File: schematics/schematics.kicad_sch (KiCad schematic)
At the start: 40 parts, among them SW1 Reset, U4 PIC32MX170F256B

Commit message: Add motor STL
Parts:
- added D? (x2): Diode, symbol 218:Diode
- added L?: Inductor, symbol 218 spdl:Inductor
- added R_ext?: 22, symbol 218 spdl:Res1
- added R_int?: 34, symbol 218 spdl:Res1
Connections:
- net +5V: now also D?.1 (K)
- net GNDREF: now also D?.2 (A), R_ext?.2
- new net: L?.2, R_int?.1
- new net PWM (7544): D?.1 (K), D?.2 (A), L?.1
- new net Probe: R_ext?.1, R_int?.2
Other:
- note added: "Lab 7.1"
- note added: "Motor"

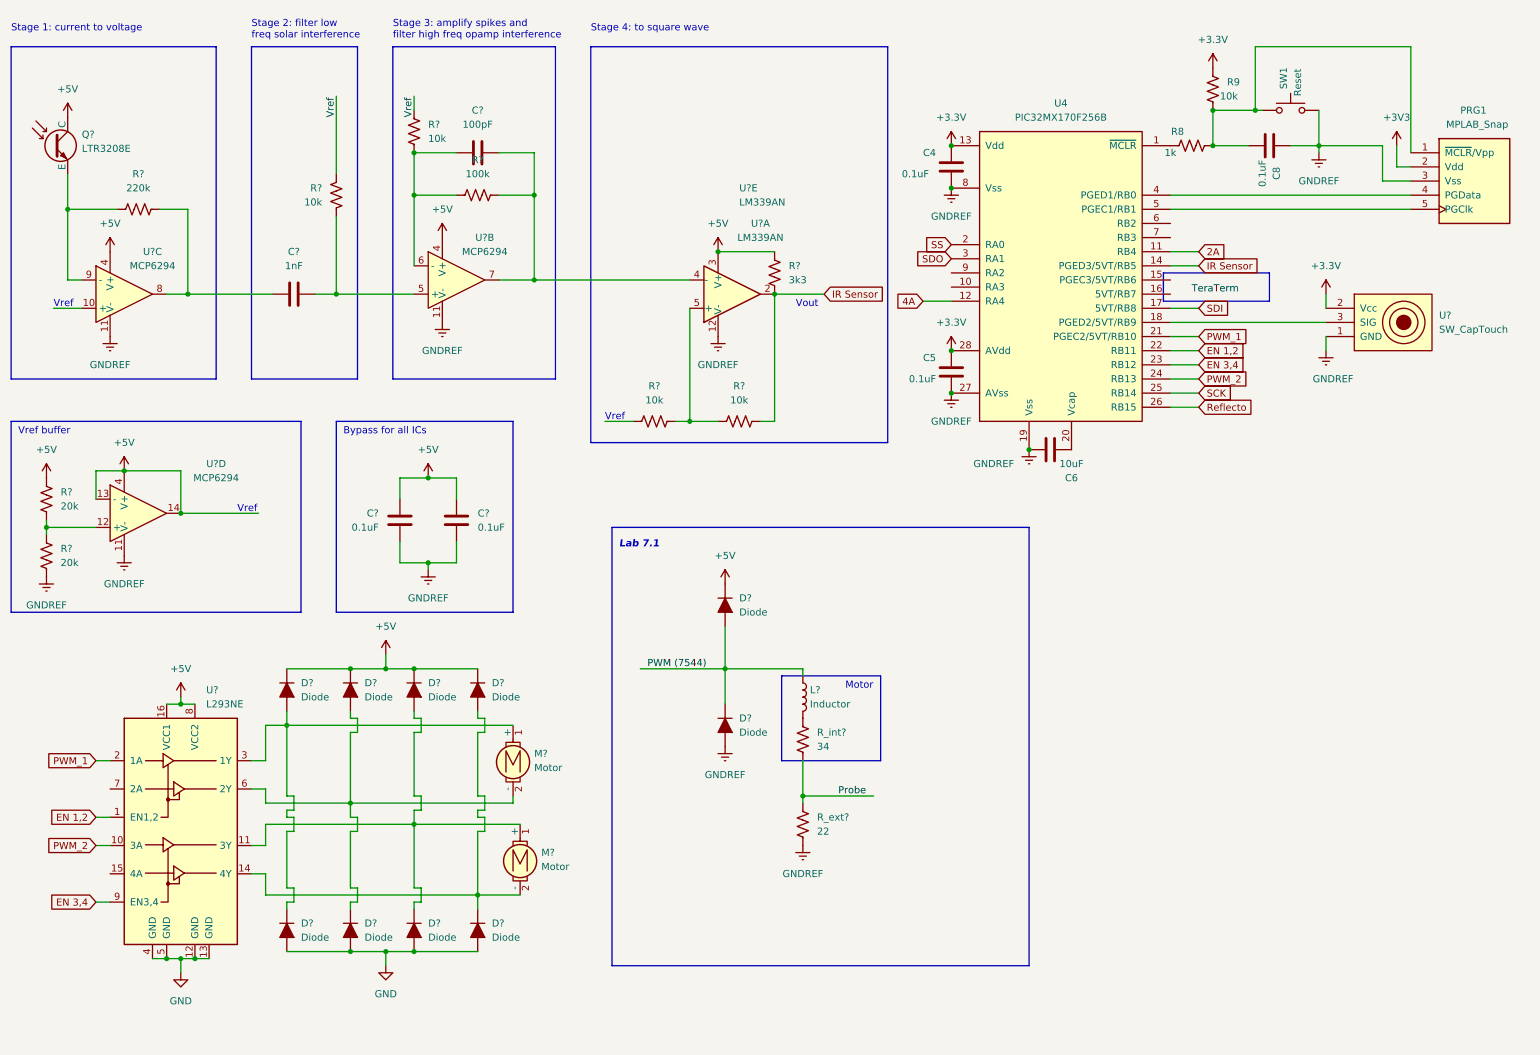
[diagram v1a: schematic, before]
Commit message: Update schematics and add new symbols to KiCAD
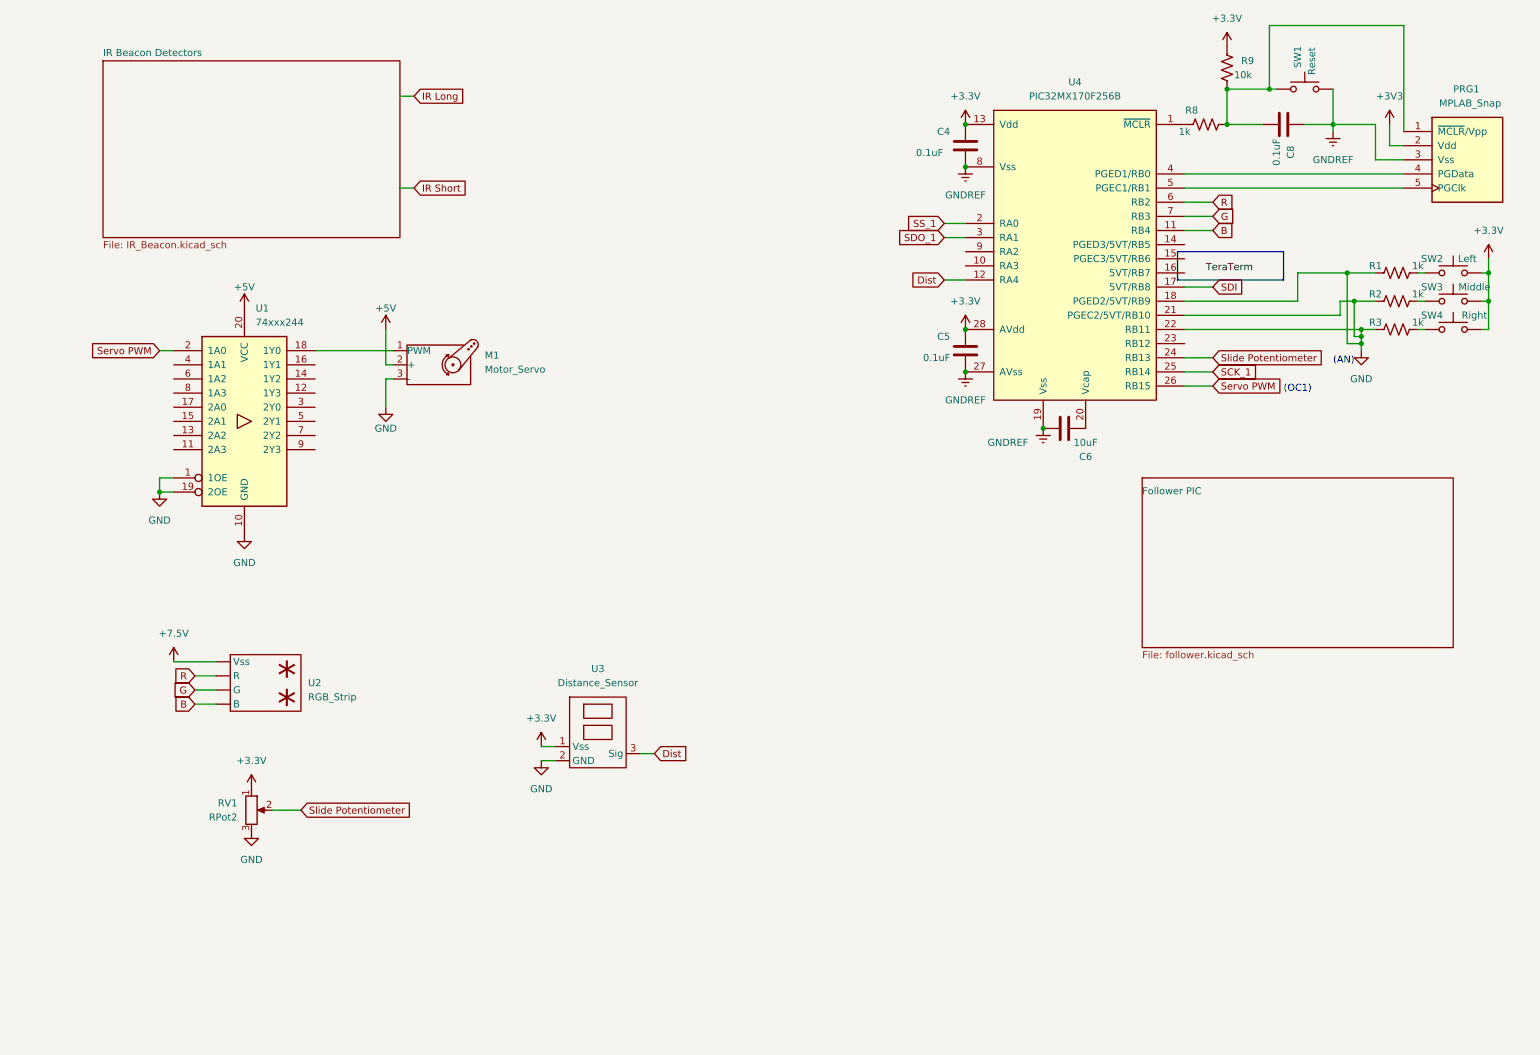
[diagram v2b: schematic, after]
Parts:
- removed C? (x2): 0.1uF, symbol ME218_BaseLib:Cap
- removed C?: 100pF, symbol ME218_BaseLib:Cap
- removed C?: 1nF, symbol ME218_BaseLib:Cap
- removed D? (x8): Diode, symbol 218 spdl:Diode
- removed D? (x2): Diode, symbol 218:Diode
- removed L?: Inductor, symbol 218 spdl:Inductor
- removed M? (x2): Motor, symbol 218 spdl:Motor
- removed Q?: LTR3208E, symbol ME218_BaseLib:Photo_NPN
- removed R?: 100k, symbol ME218_BaseLib:Res1
- removed R? (x2): 20k, symbol ME218_BaseLib:Res1
- removed R? (x4): 10k, symbol ME218_BaseLib:Res1
- removed R?: 220k, symbol ME218_BaseLib:Res1
- removed R?: 3k3, symbol ME218_BaseLib:Res1
- removed R_ext?: 22, symbol 218 spdl:Res1
- removed R_int?: 34, symbol 218 spdl:Res1
- removed U? (x2): LM339AN, symbol ME218_BaseLib:LM339AN
- removed U? (x3): MCP6294, symbol ME218_BaseLib:MCP6294
- removed U?: SW_CapTouch, symbol 218 spdl:SW_CapTouch
- removed U?: L293NE, Package_DIP:DIP-16_W7.62mm, symbol 218 spdl:L293NE
- added M1: Motor_Servo, symbol 218 spdl:Motor_Servo
- added R1, R2, R3: 1k, symbol 218 spdl:Res1
- added RV1: RPot2, symbol 218 spdl:RPot2
- added SW2: Left, symbol 218 spdl:SW_Push
- added SW3: Middle, symbol 218 spdl:SW_Push
- added SW4: Right, symbol 218 spdl:SW_Push
- added U1: 74xxx244, symbol 218 spdl:74xxx244
- added U2: RGB_Strip, symbol Custom_Library:RGB_Strip
- added U3: Distance_Sensor, symbol Custom_Library:Distance_Sensor
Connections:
- net EN 1,2 is gone; now on net GND: U4.22 (RB11)
- net PWM_1 is gone; now on net GND: U4.21 (PGEC2/5VT/RB10)
- net +3.3V: now also RV1.1, SW2.2, SW3.2, SW4.2, U3.1 (Vss)
- net +5V: now also M1.2 (+), U1.20 (VCC)
- net GND: now also U4.18 (PGED2/5VT/RB9), M1.3 (-), R1.1, R2.1, R3.1, RV1.3, U1.1 (1OE), U1.10 (GND), U1.19 (2OE), U3.2 (GND)
- net R: now reaches U4.6 (RB2)
- net R: now also U2. (Vss)
- net G: now reaches U4.7 (RB3)
- net G: now also U2. (Vss)
- net 2A renamed B
- net B: now also U2. (Vss)
- net 4A renamed Dist
- net Dist: now also U3.3 (Sig)
- net EN 3,4: no longer names the net of U4.23 (RB12)
- net IR Sensor: no longer names the net of U4.14 (PGED3/5VT/RB5)
- net PWM_2 renamed Slide Potentiometer
- net Slide Potentiometer: now also RV1.2
- net Reflecto renamed Servo PWM
- net Servo PWM: now also U1.2 (1A0)
- net SCK renamed SCK_1
- net SDO renamed SDO_1
- net SS renamed SS_1
- new net: M1.1 (PWM), U1.18 (1Y0)
- new net: R3.2, SW4.1
- new net: R2.2, SW3.1
- new net: R1.2, SW2.1
- new net +7.5V: U2. (Vss)
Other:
- added sheet Follower PIC (follower.kicad_sch)
- added sheet IR Beacon Detectors (IR_Beacon.kicad_sch)
- note added: "(AN)"
- note added: "(OC1)"
- note removed: "Bypass for all ICs"
- note removed: "Lab 7.1"
- note removed: "Motor"
- note removed: "Stage 1: current to voltage"
- note removed: "Stage 2: filter low freq solar interference"
- note removed: "Stage 3: amplify spikes and filter high freq opamp interference"
- note removed: "Stage 4: to square wave"
- note removed: "Vout"
- note removed: "Vref"
- note removed: "Vref buffer"
- moved on the sheet: C4, C5, C6, C8, PRG1, R8, R9, SW1, U4

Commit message: Use 4 position switches to determine branch and how far to drive in KiCAD
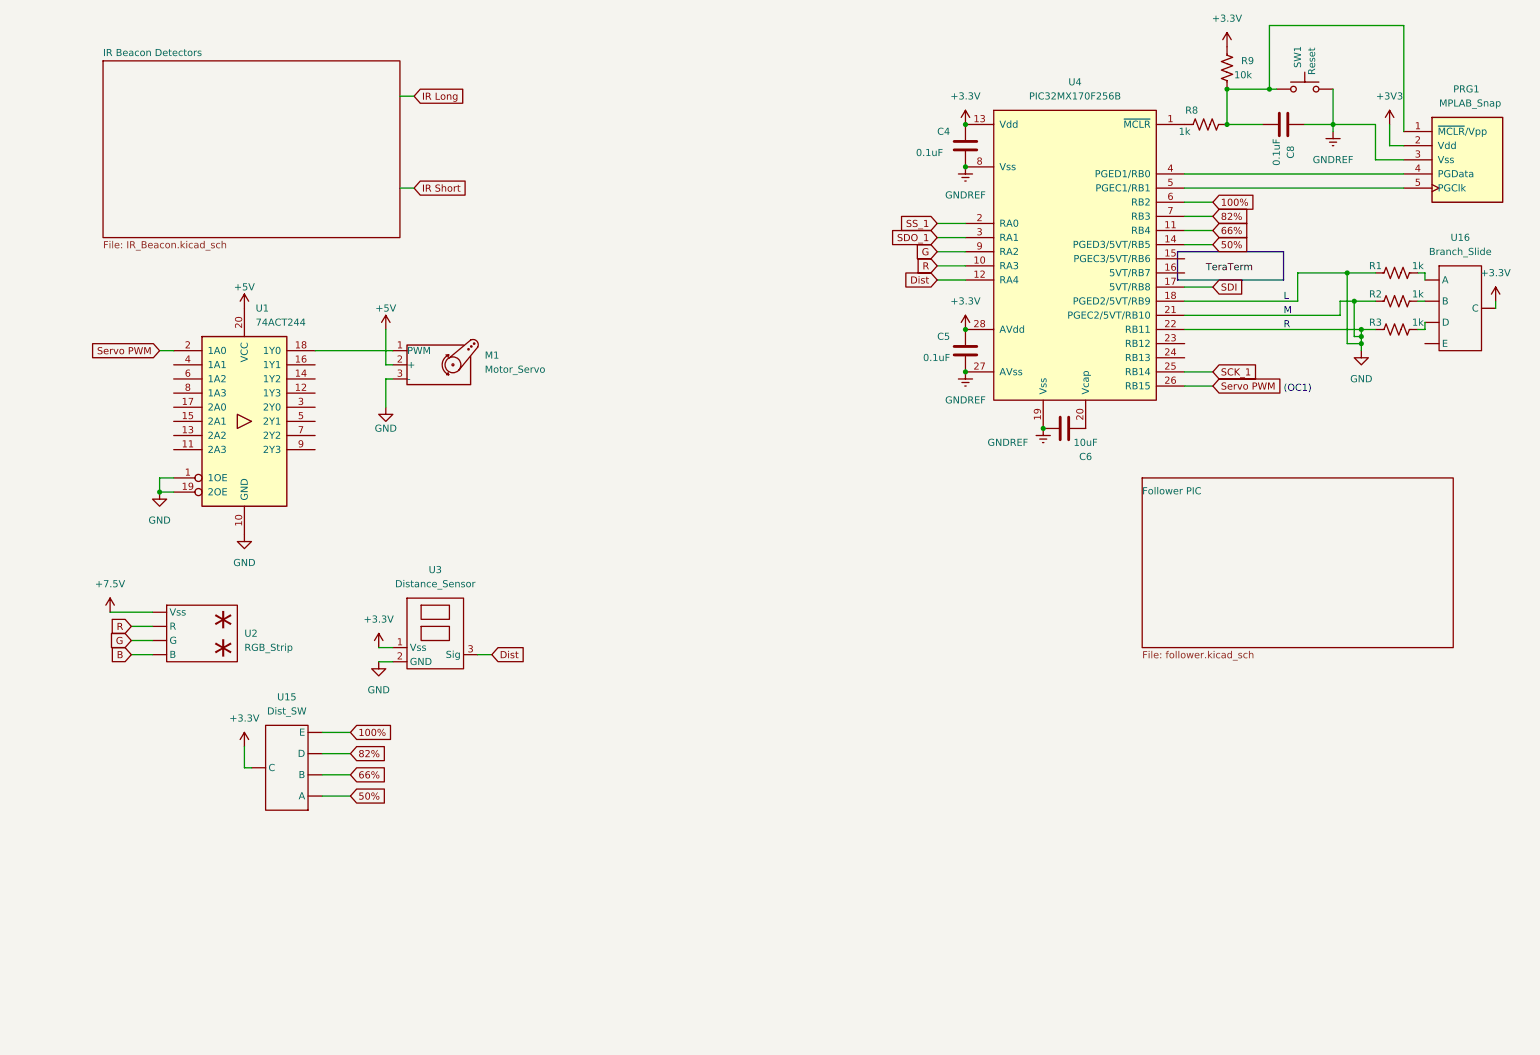
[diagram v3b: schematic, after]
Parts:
- removed RV1: RPot2, symbol 218 spdl:RPot2
- removed SW2: Left, symbol 218 spdl:SW_Push
- removed SW3: Middle, symbol 218 spdl:SW_Push
- removed SW4: Right, symbol 218 spdl:SW_Push
- added U15: Dist_SW, symbol Custom_Library:Slide_SW
- added U16: Branch_Slide, symbol Custom_Library:Slide_SW
- U1: value 74xxx244 -> 74ACT244
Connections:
- net +3.3V: now also U15. (E), U16. (E)
- net B: no longer U4.11 (RB4)
- net G: now also U4.9 (RA2); no longer U4.7 (RB3)
- net R: now also U4.10 (RA3); no longer U4.6 (RB2)
- net at R3.2: now also U16. (E)
- net 50%: now reaches U4.14 (PGED3/5VT/RB5)
- net 50%: now also U15. (E)
- net at R2.2: now also U16. (E)
- net at R1.2: now also U16. (E)
- net Slide Potentiometer: no longer names the net of U4.24 (RB13)
- new net 100%: U15. (E), U4.6 (RB2)
- new net 66%: U15. (E), U4.11 (RB4)
- new net 82%: U15. (E), U4.7 (RB3)
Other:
- note added: "L"
- note added: "M"
- note added: "R"
- note removed: "(AN)"
- moved on the sheet: U2, U3

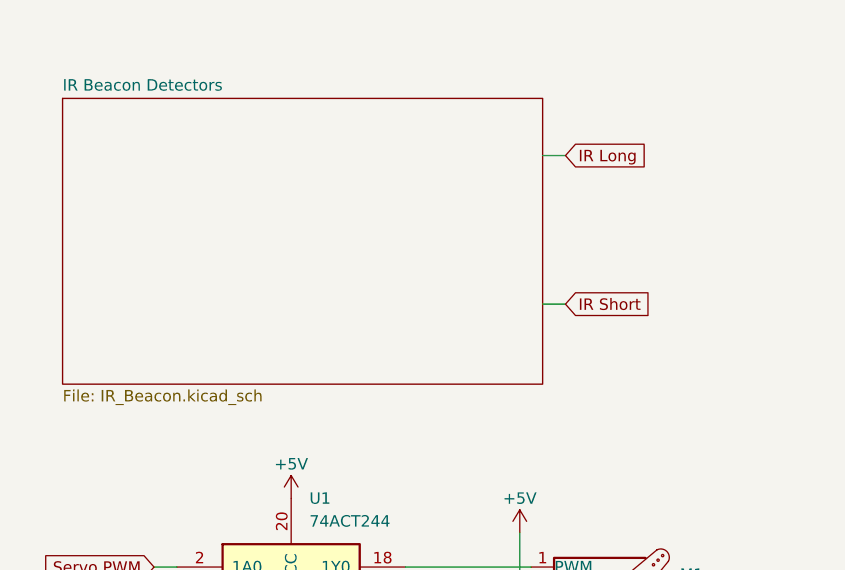
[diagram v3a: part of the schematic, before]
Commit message: Move IR sensors to follower PIC and add missing SPI PICs
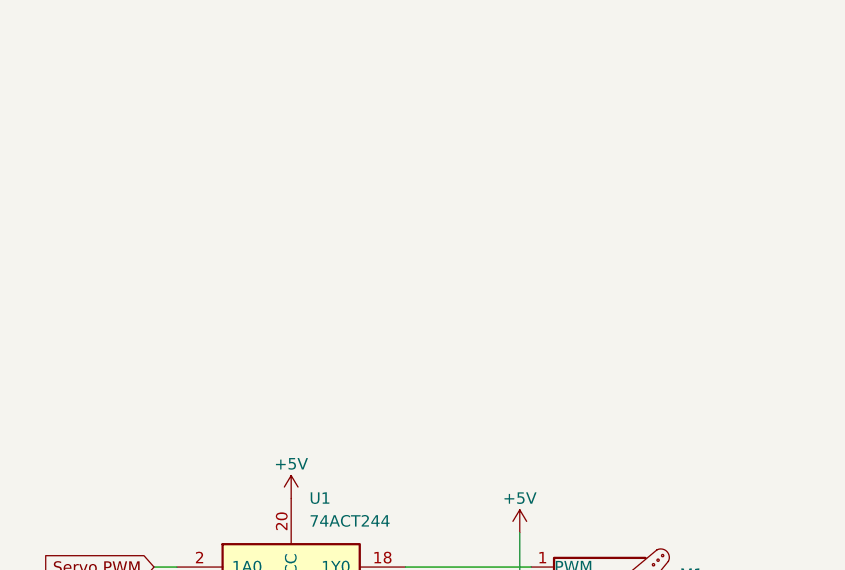
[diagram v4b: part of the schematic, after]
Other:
- removed sheet IR Beacon Detectors
